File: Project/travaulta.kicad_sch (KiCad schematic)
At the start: 26 parts, among them SW38 BOOT0, U1 STM32F401CBUx, U2 XC6206PxxxMR, Y1 8 MHz

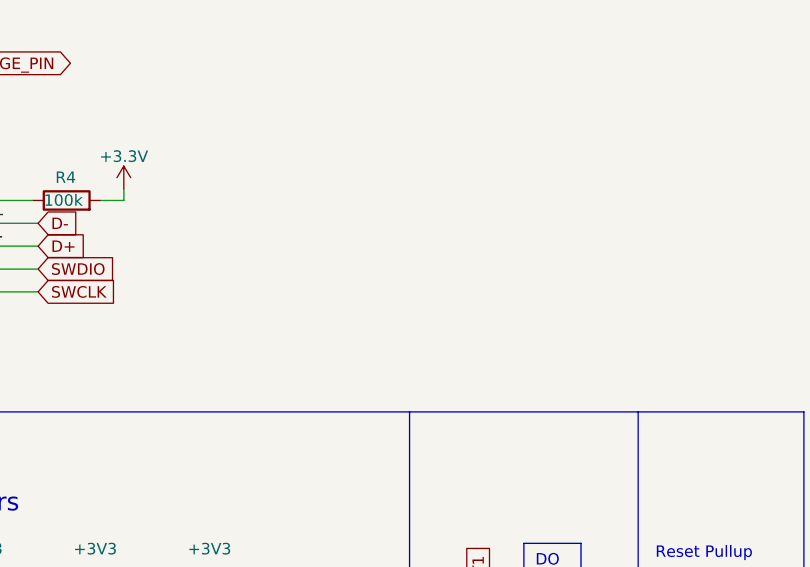
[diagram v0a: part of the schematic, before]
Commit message: add daughterboard header
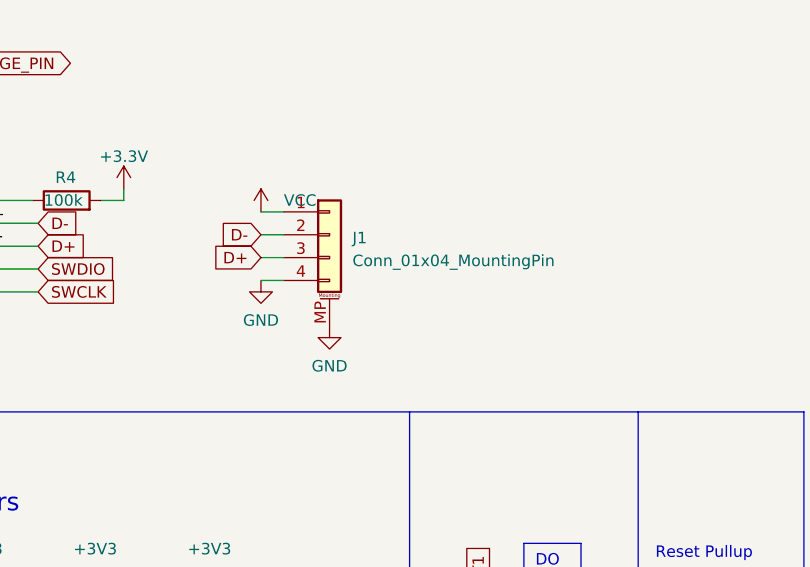
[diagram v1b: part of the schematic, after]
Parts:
- added J1: Conn_01x04_MountingPin, Connector_JST:JST_SH_SM04B-SRSS-TB_1x04-1MP_P1.00mm_Horizontal, symbol Connector_Generic_MountingPin:Conn_01x04_MountingPin
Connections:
- net D+: now also J1.3 (Pin_3)
- net D-: now also J1.2 (Pin_2)
- net GND: now also J1.4 (Pin_4), J1.MP (MountPin)
- net VCC: now also J1.1 (Pin_1)
